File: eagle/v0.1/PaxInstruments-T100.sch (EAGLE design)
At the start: 28 parts, among them J1 AVR_SPI_PRG_6PTH, U1 Attiny85

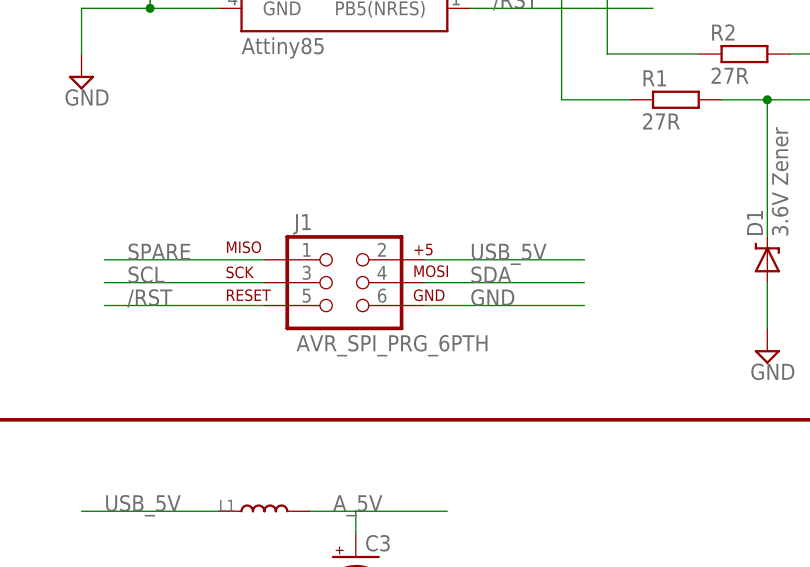
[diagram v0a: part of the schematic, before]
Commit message: ISP connector is modified.
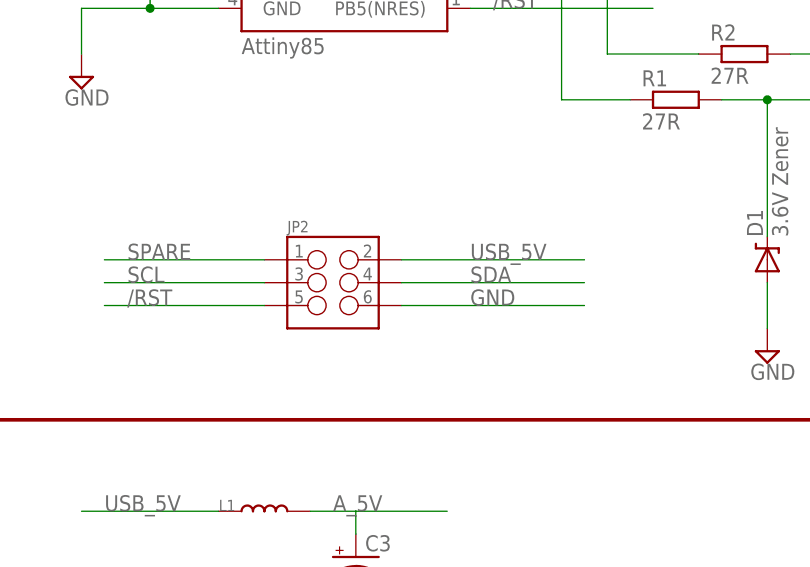
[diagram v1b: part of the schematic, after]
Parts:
- removed J1: AVR_SPI_PRG_6PTH, SparkFun-Connectors:AVR_SPI_PRG_6PTH
- added JP2: (no value), SparkFun-Connectors:M03X2SMT
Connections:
- net /RST: now also JP2.5; no longer J1.5
- net GND: now also JP2.6; no longer J1.6
- net SCL: now also JP2.3; no longer J1.3
- net SDA: now also JP2.4; no longer J1.4
- net SPARE: now also JP2.1; no longer J1.1
- net USB_5V: now also JP2.2; no longer J1.2
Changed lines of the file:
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@@
 <grid distance="0.1" unitdist="inch" unit="inch" style="lines" multiple="1" display="no" altdistance="0.01" altunitdist="inch" altunit="inch"/>
 <layers>
-<layer number="1" name="Top" color="4" fill="1" visible="yes" active="no"/>
-<layer number="16" name="Bottom" color="1" fill="1" visible="yes" active="no"/>
-<layer number="17" name="Pads" color="2" fill="1" visible="yes" active="no"/>
-<layer number="18" name="Vias" color="2" fill="1" visible="yes" active="no"/>
-<layer number="19" name="Unrouted" color="6" fill="1" visible="yes" active="no"/>
-<layer number="20" name="Dimension" color="15" fill="1" visible="yes" active="no"/>
-<layer number="21" name="tPlace" color="7" fill="1" visible="yes" active="no"/>
-<layer number="22" name="bPlace" color="7" fill="1" visible="yes" active="no"/>
-<layer number="23" name="tOrigins" color="15" fill="1" visible="yes" active="no"/>
-<layer number="24" name="bOrigins" color="15" fill="1" visible="yes" active="no"/>
-<layer number="25" name="tNames" color="7" fill="1" visible="yes" active="no"/>
-<layer number="26" name="bNames" color="7" fill="1" visible="yes" active="no"/>
-<layer number="27" name="tValues" color="7" fill="1" visible="yes" active="no"/>
-<layer number="28" name="bValues" color="7" fill="1" visible="yes" active="no"/>
+<layer number="1" name="Top" color="4" fill="1" visible="no" active="no"/>
+<layer number="16" name="Bottom" color="1" fill="1" visible="no" active="no"/>
+<layer number="17" name="Pads" color="2" fill="1" visible="no" active="no"/>
+<layer number="18" name="Vias" color="2" fill="1" visible="no" active="no"/>
+<layer number="19" name="Unrouted" color="6" fill="1" visible="no" active="no"/>
+<layer number="20" name="Dimension" color="15" fill="1" visible="no" active="no"/>
+<layer number="21" name="tPlace" color="7" fill="1" visible="no" active="no"/>
+<layer number="22" name="bPlace" color="7" fill="1" visible="no" active="no"/>
+<layer number="23" name="tOrigins" color="15" fill="1" visible="no" active="no"/>
+<layer number="24" name="bOrigins" color="15" fill="1" visible="no" active="no"/>
+<layer number="25" name="tNames" color="7" fill="1" visible="no" active="no"/>
+<layer number="26" name="bNames" color="7" fill="1" visible="no" active="no"/>
+<layer number="27" name="tValues" color="7" fill="1" visible="no" active="no"/>
+<layer number="28" name="bValues" color="7" fill="1" visible="no" active="no"/>
 <layer number="29" name="tStop" color="7" fill="3" visible="no" active="no"/>
 <layer number="30" name="bStop" color="7" fill="6" visible="no" active="no"/>
@@
 <layer number="35" name="tGlue" color="7" fill="4" visible="no" active="no"/>
 <layer number="36" name="bGlue" color="7" fill="5" visible="no" active="no"/>
-<layer number="37" name="tTest" color="7" fill="1" visible="yes" active="no"/>
-<layer number="38" name="bTest" color="7" fill="1" visible="yes" active="no"/>
+<layer number="37" name="tTest" color="7" fill="1" visible="no" active="no"/>
+<layer number="38" name="bTest" color="7" fill="1" visible="no" active="no"/>
 <layer number="39" name="tKeepout" color="4" fill="11" visible="no" active="no"/>
 <layer number="40" name="bKeepout" color="1" fill="11" visible="no" active="no"/>
@@
 <layer number="44" name="Drills" color="7" fill="1" visible="no" active="no"/>
 <layer number="45" name="Holes" color="7" fill="1" visible="no" active="no"/>
-<layer number="46" name="Milling" color="3" fill="1" visible="yes" active="no"/>
-<layer number="47" name="Measures" color="7" fill="1" visible="yes" active="no"/>
-<layer number="48" name="Document" color="7" fill="1" visible="yes" active="no"/>
-<layer number="49" name="Reference" color="7" fill="1" visible="yes" active="no"/>
-<layer number="50" name="dxf" color="7" fill="1" visible="yes" active="no"/>
-<layer number="51" name="tDocu" color="7" fill="1" visible="yes" active="no"/>
-<layer number="52" name="bDocu" color="7" fill="1" visible="yes" active="no"/>
-<layer number="53" name="tGND_GNDA" color="7" fill="9" visible="yes" active="no"/>
-<layer number="54" name="bGND_GNDA" color="1" fill="9" visible="yes" active="no"/>
-<layer number="56" name="wert" color="7" fill="1" visible="yes" active="no"/>
+<layer number="46" name="Milling" color="3" fill="1" visible="no" active="no"/>
+<layer number="47" name="Measures" color="7" fill="1" visible="no" active="no"/>
+<layer number="48" name="Document" color="7" fill="1" visible="no" active="no"/>
+<layer number="49" name="Reference" color="7" fill="1" visible="no" active="no"/>
+<layer number="50" name="dxf" color="7" fill="1" visible="no" active="no"/>
+<layer number="51" name="tDocu" color="7" fill="1" visible="no" active="no"/>
+<layer number="52" name="bDocu" color="7" fill="1" visible="no" active="no"/>
+<layer number="53" name="tGND_GNDA" color="7" fill="9" visible="no" active="no"/>
+<layer number="54" name="bGND_GNDA" color="1" fill="9" visible="no" active="no"/>
+<layer number="56" name="wert" color="7" fill="1" visible="no" active="no"/>
 <layer number="90" name="Modules" color="5" fill="1" visible="yes" active="yes"/>
 <layer number="91" name="Nets" color="2" fill="1" visible="yes" active="yes"/>
@@
 <part name="C2" library="SparkFun-Capacitors" deviceset="10UF-TANT" device="" value="10uF"/>
 <part name="SUPPLY5" library="supply2" deviceset="GND" device=""/>
-<part name="J1" library="SparkFun-Connectors" deviceset="AVR_SPI_PRG_6" device="PTH"/>
 <part name="LOGO1" library="SparkFun-Aesthetics" deviceset="OSHW-LOGO" device="S" value="OSHW-LOGOS"/>
 <part name="U$1" library="charlespax" deviceset="PAX-LOGO" device=""/>
@@
 <part name="R7" library="rcl" deviceset="R-EU_" device="R0603" value="4.7k"/>
 <part name="R8" library="rcl" deviceset="R-EU_" device="R0603" value="4.7k"/>
+<part name="JP2" library="SparkFun-Connectors" deviceset="M03X2" device="SMT"/>
 </parts>
 <sheets>
@@
 <instance part="C2" gate="G$1" x="129.54" y="129.54"/>
 <instance part="SUPPLY5" gate="GND" x="129.54" y="114.3"/>
-<instance part="J1" gate="G$1" x="43.18" y="121.92"/>
 <instance part="LOGO1" gate="G$1" x="175.26" y="15.24"/>
 <instance part="U$1" gate="G$1" x="193.04" y="12.7"/>
@@
 <instance part="R7" gate="G$1" x="226.06" y="48.26" rot="R90"/>
 <instance part="R8" gate="G$1" x="238.76" y="48.26" rot="R90"/>
+<instance part="JP2" gate="G$1" x="43.18" y="121.92"/>
 </instances>
 <busses>
@@
 </segment>
 <segment>
-<pinref part="J1" gate="G$1" pin="2"/>
-<wire x1="53.34" y1="124.46" x2="71.12" y2="124.46" width="0.1524" layer="91"/>
+<wire x1="50.8" y1="124.46" x2="71.12" y2="124.46" width="0.1524" layer="91"/>
 <label x="58.42" y="124.46" size="1.778" layer="95"/>
+<pinref part="JP2" gate="G$1" pin="2"/>
 </segment>
 <segment>
@@
 </segment>
 <segment>
-<pinref part="J1" gate="G$1" pin="6"/>
-<wire x1="53.34" y1="119.38" x2="71.12" y2="119.38" width="0.1524" layer="91"/>
+<wire x1="50.8" y1="119.38" x2="71.12" y2="119.38" width="0.1524" layer="91"/>
 <label x="58.42" y="119.38" size="1.778" layer="95"/>
+<pinref part="JP2" gate="G$1" pin="6"/>
 </segment>
 <segment>
@@
 </segment>
 <segment>
-<pinref part="J1" gate="G$1" pin="5"/>
 <wire x1="35.56" y1="119.38" x2="17.78" y2="119.38" width="0.1524" layer="91"/>
 <label x="20.32" y="119.38" size="1.778" layer="95"/>
+<pinref part="JP2" gate="G$1" pin="5"/>
 </segment>
 </net>
@@
 </segment>
 <segment>
-<pinref part="J1" gate="G$1" pin="3"/>
 <wire x1="35.56" y1="121.92" x2="17.78" y2="121.92" width="0.1524" layer="91"/>
 <label x="20.32" y="121.92" size="1.778" layer="95"/>
+<pinref part="JP2" gate="G$1" pin="3"/>
 </segment>
 <segment>
@@
 </segment>
 <segment>
-<pinref part="J1" gate="G$1" pin="1"/>
 <wire x1="35.56" y1="124.46" x2="17.78" y2="124.46" width="0.1524" layer="91"/>
 <label x="20.32" y="124.46" size="1.778" layer="95"/>
+<pinref part="JP2" gate="G$1" pin="1"/>
 </segment>
 </net>
@@
 </segment>
 <segment>
-<pinref part="J1" gate="G$1" pin="4"/>
-<wire x1="53.34" y1="121.92" x2="71.12" y2="121.92" width="0.1524" layer="91"/>
+<wire x1="50.8" y1="121.92" x2="71.12" y2="121.92" width="0.1524" layer="91"/>
 <label x="58.42" y="121.92" size="1.778" layer="95"/>
-</segment>
-<segment>
+<pinref part="JP2" gate="G$1" pin="4"/>
+</segment>
+<segment>
